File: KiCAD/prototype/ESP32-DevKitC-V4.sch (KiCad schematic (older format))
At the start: 31 parts

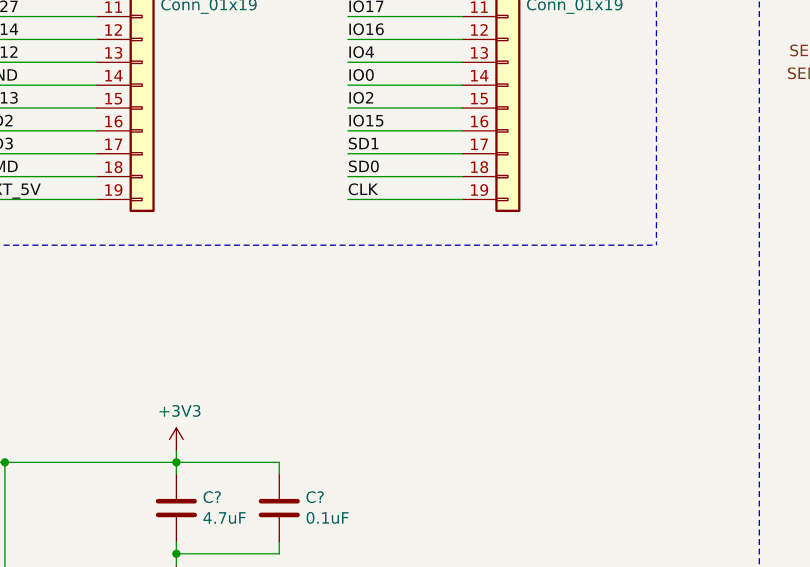
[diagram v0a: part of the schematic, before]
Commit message: Correction of miss placed folder
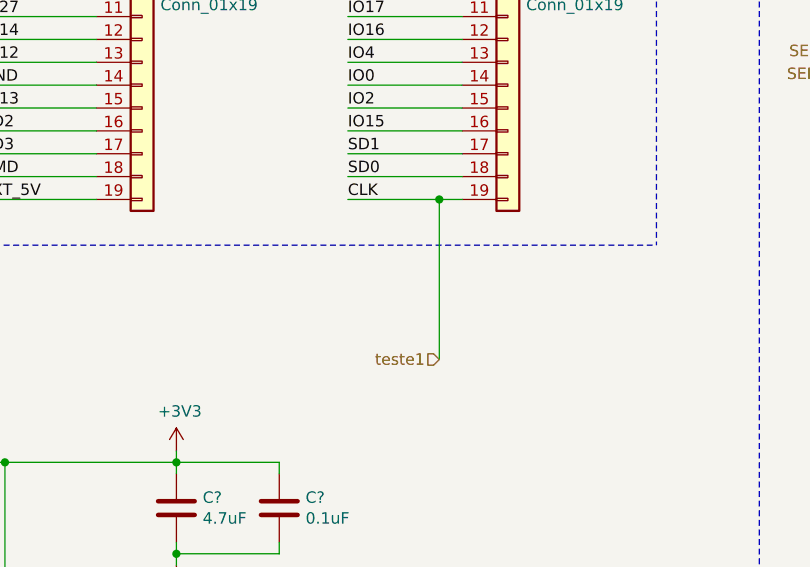
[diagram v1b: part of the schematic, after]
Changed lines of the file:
@@
 $Descr A4 11693 8268
 encoding utf-8
-Sheet 2 2
+Sheet 2 6
 Title "ESP32-DevKitC-V4"
 Date "2020-10-23"
@@
 	6550 2600 6050 2600
 Wire Wire Line
-	6550 2700 6050 2700
+	6550 2700 6450 2700
 Text Label 6050 900  0    50   ~ 0
 GND
@@
 Wire Wire Line
 	5050 4850 5500 4850
+Text HLabel 6450 3400 0    50   Input ~ 0
+teste1
+Wire Wire Line
+	6450 3400 6450 2700
+Connection ~ 6450 2700
+Wire Wire Line
+	6450 2700 6050 2700
 $EndSCHEMATC
